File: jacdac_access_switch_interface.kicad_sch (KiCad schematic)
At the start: 42 parts

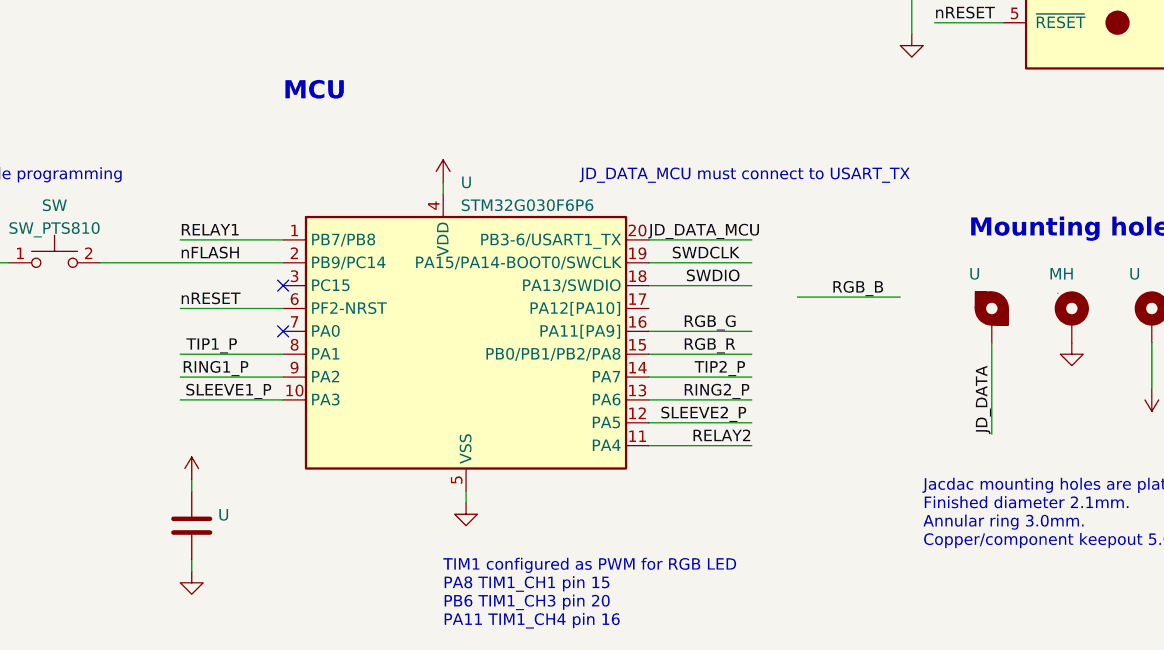
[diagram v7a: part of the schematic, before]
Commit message: Reassigned pins on MCU and spun MCU, routing ongoing
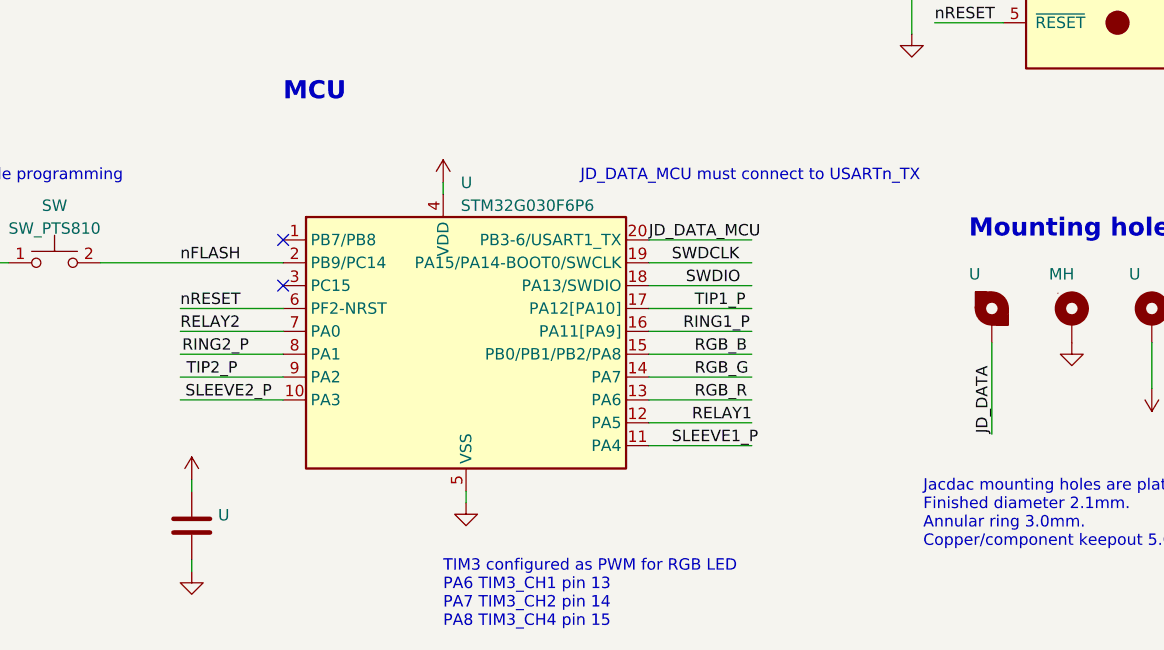
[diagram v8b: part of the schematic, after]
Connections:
- net RELAY1: now also U.12 (PA5); no longer U.1 (PB7/PB8)
- net RELAY2: now also U.7 (PA0); no longer U.11 (PA4)
- net RGB_B: now also U.15 (PB0/PB1/PB2/PA8)
- net RGB_G: now also U.14 (PA7); no longer U.16 (PA11[PA9])
- net RGB_R: now also U.13 (PA6); no longer U.15 (PB0/PB1/PB2/PA8)
- net RING1_P: now also U.16 (PA11[PA9]); no longer U.9 (PA2)
- net RING2_P: now also U.8 (PA1); no longer U.13 (PA6)
- net SLEEVE1_P: now also U.11 (PA4); no longer U.10 (PA3)
- net SLEEVE2_P: now also U.10 (PA3); no longer U.12 (PA5)
- net TIP1_P: now also U.17 (PA12[PA10]); no longer U.8 (PA1)
- net TIP2_P: now also U.9 (PA2); no longer U.14 (PA7)
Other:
- note added: "JD_DATA_MCU must connect to USARTn_TX"
- note added: "TIM3 configured as PWM for RGB LED PA6 TIM3_CH1 pin 13 PA7 TIM3_CH2 pin 14 PA8 TIM3_CH4 pin 15"
- note removed: "JD_DATA_MCU must connect to USART_TX"
- note removed: "TIM1 configured as PWM for RGB LED PA8 TIM1_CH1 pin 15 PB6 TIM1_CH3 pin 20 PA11 TIM1_CH4 pin 16"
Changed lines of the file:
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@@
   (junction (at 44.45 40.64) (diameter 0) (color 0 0 0 0)
   )
-  (no_connect (at 50.8 163.83))
+  (no_connect (at 50.8 153.67))
   (no_connect (at 50.8 158.75))
+  (wire (pts (xy 91.44 163.83) (xy 102.87 163.83))
+    (stroke (width 0) (type default))
+  )
   (wire (pts (xy 91.44 171.45) (xy 102.87 171.45))
     (stroke (width 0) (type default))
   )
-  (wire (pts (xy 107.95 160.02) (xy 119.38 160.02))
-    (stroke (width 0) (type default))
-  )
   (wire (pts (xy 172.72 78.74) (xy 175.26 78.74))
     (stroke (width 0) (type default))
@@
     (stroke (width 0) (type default))
   )
-  (wire (pts (xy 39.37 153.67) (xy 50.8 153.67))
+  (wire (pts (xy 39.37 163.83) (xy 50.8 163.83))
     (stroke (width 0) (type default))
   )
@@
     (stroke (width 0) (type default))
   )
-  (wire (pts (xy 91.44 163.83) (xy 102.87 163.83))
+  (wire (pts (xy 91.44 168.91) (xy 102.87 168.91))
     (stroke (width 0) (type default))
   )
@@
     (stroke (width 0) (type default))
   )
-  (wire (pts (xy 91.44 168.91) (xy 102.87 168.91))
+  (wire (pts (xy 91.44 161.29) (xy 102.87 161.29))
     (stroke (width 0) (type default))
   )
@@
     (effects (font (size 1.27 1.27)) (justify right bottom))
   )
-  (text "JD_DATA_MCU must connect to USART_TX" (at 83.82 147.32 0)
+  (text "JD_DATA_MCU must connect to USARTn_TX" (at 83.82 147.32 0)
     (effects (font (size 1.27 1.27)) (justify left bottom))
   )
@@
     (effects (font (size 2.0066 2.0066) (thickness 0.4013) bold) (justify left bottom))
   )
-  (text "TIM1 configured as PWM for RGB LED\nPA8 TIM1_CH1 pin 15\nPB6 TIM1_CH3 pin 20\nPA11 TIM1_CH4 pin 16\n"
+  (text "TIM3 configured as PWM for RGB LED\nPA6 TIM3_CH1 pin 13\nPA7 TIM3_CH2 pin 14\nPA8 TIM3_CH4 pin 15\n"
     (at 68.58 196.85 0)
     (effects (font (size 1.27 1.27)) (justify left bottom))
@@
     (effects (font (size 1.27 1.27)) (justify left bottom))
   )
-  (label "RELAY1" (at 39.37 153.67 0) (fields_autoplaced)
+  (label "RELAY2" (at 39.37 163.83 0) (fields_autoplaced)
     (effects (font (size 1.27 1.27)) (justify left bottom))
   )
@@
     (effects (font (size 1.27 1.27)) (justify left bottom))
   )
-  (label "SLEEVE1_P" (at 49.53 171.45 0) (fields_autoplaced)
+  (label "SLEEVE2_P" (at 49.53 171.45 0) (fields_autoplaced)
     (effects (font (size 1.27 1.27)) (justify right bottom))
   )
@@
     (effects (font (size 1.27 1.27)) (justify left bottom))
   )
-  (label "RING1_P" (at 46.99 168.91 0) (fields_autoplaced)
+  (label "RING2_P" (at 46.99 166.37 0) (fields_autoplaced)
     (effects (font (size 1.27 1.27)) (justify right bottom))
   )
@@
     (effects (font (size 1.27 1.27)) (justify right bottom))
   )
-  (label "RGB_R" (at 95.25 166.37 0) (fields_autoplaced)
+  (label "RGB_R" (at 96.52 171.45 0) (fields_autoplaced)
     (effects (font (size 1.27 1.27)) (justify left bottom))
   )
@@
     (effects (font (size 1.27 1.27)) (justify left bottom))
   )
-  (label "RGB_G" (at 95.25 163.83 0) (fields_autoplaced)
+  (label "RGB_G" (at 96.52 168.91 0) (fields_autoplaced)
     (effects (font (size 1.27 1.27)) (justify left bottom))
   )
@@
     (effects (font (size 1.27 1.27)) (justify left bottom))
   )
-  (label "RGB_B" (at 111.76 160.02 0) (fields_autoplaced)
+  (label "RGB_B" (at 96.52 166.37 0) (fields_autoplaced)
     (effects (font (size 1.27 1.27)) (justify left bottom))
   )
@@
     (effects (font (size 1.27 1.27)) (justify left bottom))
   )
-  (label "SLEEVE2_P" (at 92.71 173.99 0) (fields_autoplaced)
+  (label "SLEEVE1_P" (at 93.98 176.53 0) (fields_autoplaced)
     (effects (font (size 1.27 1.27)) (justify left bottom))
   )
@@
     (effects (font (size 1.27 1.27)) (justify left bottom))
   )
-  (label "TIP1_P" (at 45.72 166.37 0) (fields_autoplaced)
+  (label "TIP2_P" (at 45.72 168.91 0) (fields_autoplaced)
     (effects (font (size 1.27 1.27)) (justify right bottom))
   )
-  (label "RELAY2" (at 102.87 176.53 0) (fields_autoplaced)
+  (label "RELAY1" (at 102.87 173.99 0) (fields_autoplaced)
     (effects (font (size 1.27 1.27)) (justify right bottom))
   )
@@
     (effects (font (size 1.27 1.27)) (justify left bottom))
   )
-  (label "RING2_P" (at 95.25 171.45 0) (fields_autoplaced)
-    (effects (font (size 1.27 1.27)) (justify left bottom))
-  )
-  (label "TIP2_P" (at 96.52 168.91 0) (fields_autoplaced)
+  (label "RING1_P" (at 95.25 163.83 0) (fields_autoplaced)
+    (effects (font (size 1.27 1.27)) (justify left bottom))
+  )
+  (label "TIP1_P" (at 96.52 161.29 0) (fields_autoplaced)
     (effects (font (size 1.27 1.27)) (justify left bottom))
   )
@@
     (pin "1")
   )
-  (symbol (lib_id "jacdac_access_switch_interface:jack_3.5mm_PJ313D") (at 138.43 30.48 0) (unit 1)
+  (symbol (lib_name "jack_3.5mm_PJ313D_1") (lib_id "jacdac_access_switch_interface:jack_3.5mm_PJ313D") (at 138.43 30.48 0) (unit 1)
     (in_bom yes) (on_board yes)
     (default_instance (reference "J") (unit 1) (value "jack_3.5_pj313d") (footprint "jacdac_access_switch_interface:jack_3.5_pj313d_smt"))
